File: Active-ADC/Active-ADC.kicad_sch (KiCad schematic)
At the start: 18 parts, among them J1 FPGA Terminal, J2 ADC Terminal, Q1 BC847, Q2 BC847, Q3 BC847

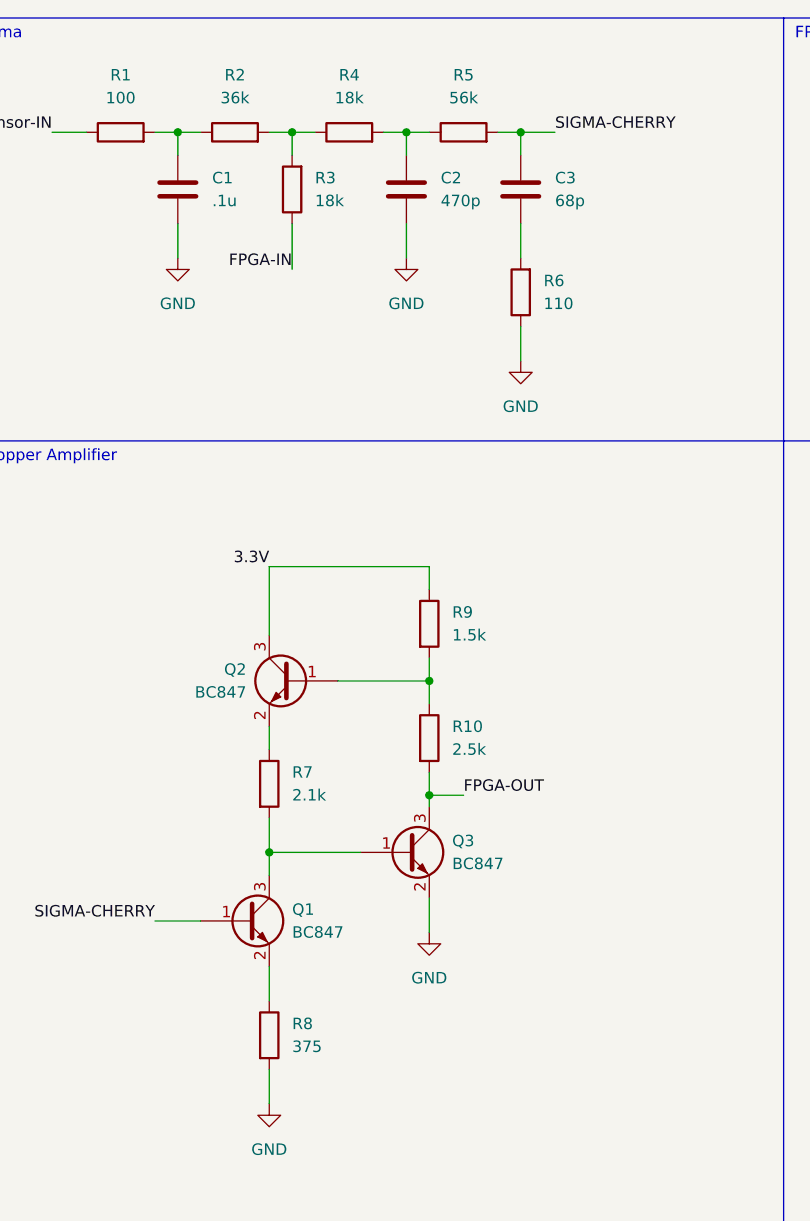
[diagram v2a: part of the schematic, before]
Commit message: Updated schematic for full SMD components with part numbers
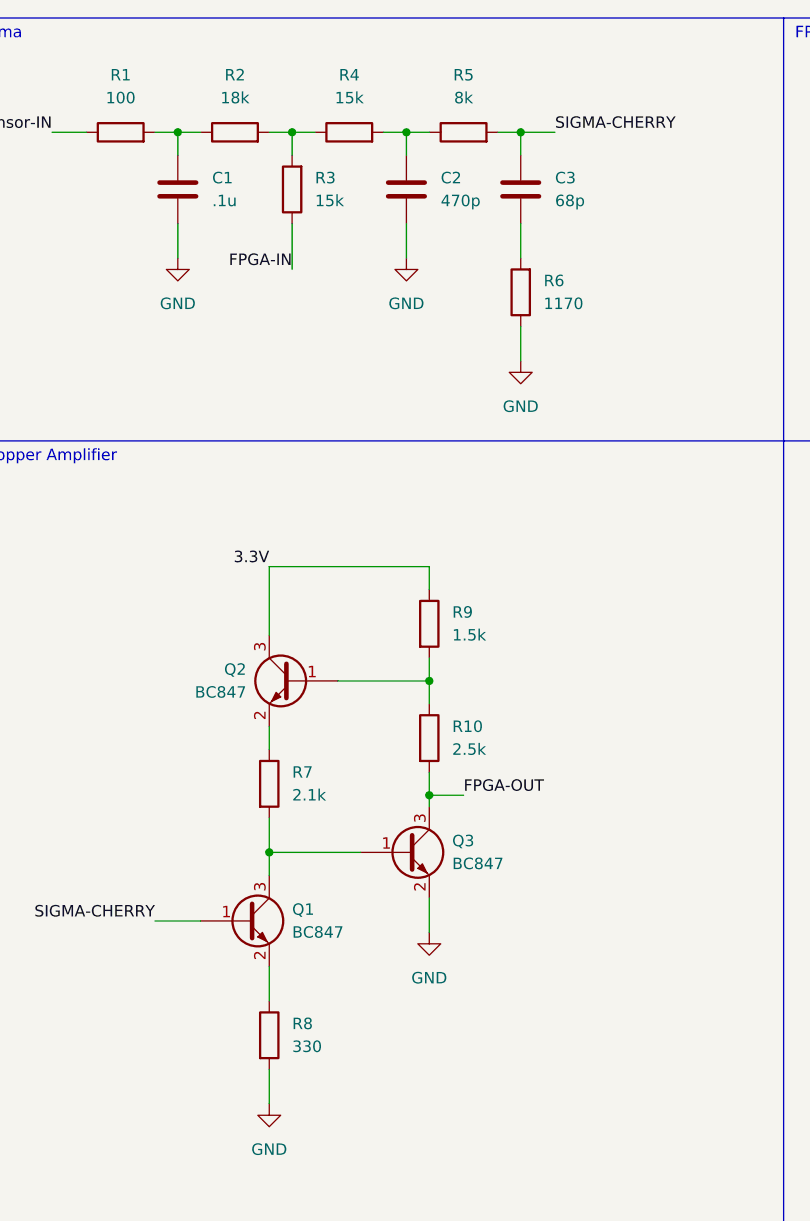
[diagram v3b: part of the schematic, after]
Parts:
- C3: footprint Capacitor_SMD:C_0402_1005Metric -> Capacitor_SMD:C_0201_0603Metric
- R10: footprint Resistor_SMD:R_0201_0603Metric -> Resistor_SMD:R_0805_2012Metric
- R2: value 36k -> 18k
- R3, R4: value 18k -> 15k
- R5: value 56k -> 8k; footprint Resistor_SMD:R_0201_0603Metric -> Resistor_SMD:R_0805_2012Metric
- R6: value 110 -> 1170
- R8: value 375 -> 330
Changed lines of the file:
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@@
     (in_bom yes) (on_board yes) (fields_autoplaced)
     (property "Reference" "R5" (id 0) (at 73.66 19.05 90))
-    (property "Value" "56k" (id 1) (at 73.66 21.59 90))
-    (property "Footprint" "Resistor_SMD:R_0201_0603Metric" (id 2) (at 73.66 27.178 90)
-      (effects (font (size 1.27 1.27)) hide)
-    )
-    (property "Datasheet" "P123347TR-ND" (id 3) (at 73.66 25.4 0)
+    (property "Value" "8k" (id 1) (at 73.66 21.59 90))
+    (property "Footprint" "Resistor_SMD:R_0805_2012Metric" (id 2) (at 73.66 27.178 90)
+      (effects (font (size 1.27 1.27)) hide)
+    )
+    (property "Datasheet" "Y1629-8.00KATR-ND" (id 3) (at 73.66 25.4 0)
       (effects (font (size 1.27 1.27)) hide)
     )
@@
       (effects (font (size 1.27 1.27)) (justify left))
     )
-    (property "Footprint" "Resistor_SMD:R_0201_0603Metric" (id 2) (at 68.072 92.71 90)
-      (effects (font (size 1.27 1.27)) hide)
-    )
-    (property "Datasheet" "~" (id 3) (at 69.85 92.71 0)
+    (property "Footprint" "Resistor_SMD:R_0805_2012Metric" (id 2) (at 68.072 92.71 90)
+      (effects (font (size 1.27 1.27)) hide)
+    )
+    (property "Datasheet" "Y1629-2.50KATR-ND" (id 3) (at 69.85 92.71 0)
       (effects (font (size 1.27 1.27)) hide)
     )
@@
       (effects (font (size 1.27 1.27)) hide)
     )
-    (property "Datasheet" "~" (id 3) (at 69.85 80.01 0)
+    (property "Datasheet" "1292-WR06X152JTLTR-ND" (id 3) (at 69.85 80.01 0)
       (effects (font (size 1.27 1.27)) hide)
     )
@@
     (in_bom yes) (on_board yes) (fields_autoplaced)
     (property "Reference" "R4" (id 0) (at 60.96 19.05 90))
-    (property "Value" "18k" (id 1) (at 60.96 21.59 90))
+    (property "Value" "15k" (id 1) (at 60.96 21.59 90))
     (property "Footprint" "Resistor_SMD:R_0201_0603Metric" (id 2) (at 60.96 27.178 90)
       (effects (font (size 1.27 1.27)) hide)
     )
-    (property "Datasheet" "311-18.0KMTR-ND" (id 3) (at 60.96 25.4 0)
+    (property "Datasheet" "1292-WR06X153JTLTR-ND" (id 3) (at 60.96 25.4 0)
       (effects (font (size 1.27 1.27)) hide)
     )
@@
       (effects (font (size 1.27 1.27)) (justify left))
     )
-    (property "Value" "375" (id 1) (at 54.61 126.9999 0)
+    (property "Value" "330" (id 1) (at 54.61 126.9999 0)
       (effects (font (size 1.27 1.27)) (justify left))
     )
@@
       (effects (font (size 1.27 1.27)) hide)
     )
-    (property "Datasheet" "~" (id 3) (at 52.07 125.73 0)
+    (property "Datasheet" "1292-WR06X331JTLTR-ND" (id 3) (at 52.07 125.73 0)
       (effects (font (size 1.27 1.27)) hide)
     )
@@
       (effects (font (size 1.27 1.27)) (justify right))
     )
-    (property "Value" "110" (id 1) (at 82.55 44.4499 0)
+    (property "Value" "1170" (id 1) (at 82.55 44.4499 0)
       (effects (font (size 1.27 1.27)) (justify right))
     )
@@
       (effects (font (size 1.27 1.27)) hide)
     )
-    (property "Datasheet" "YAG2379TR-ND" (id 3) (at 80.01 43.18 0)
+    (property "Datasheet" "2019-RN73R1JTTD1171B10TR-ND" (id 3) (at 80.01 43.18 0)
       (effects (font (size 1.27 1.27)) hide)
     )
@@
       (effects (font (size 1.27 1.27)) (justify right))
     )
-    (property "Value" "18k" (id 1) (at 57.15 33.0199 0)
+    (property "Value" "15k" (id 1) (at 57.15 33.0199 0)
       (effects (font (size 1.27 1.27)) (justify right))
     )
@@
       (effects (font (size 1.27 1.27)) hide)
     )
-    (property "Datasheet" "311-18.0KMTR-ND" (id 3) (at 54.61 31.75 0)
+    (property "Datasheet" "1292-WR06X153JTLTR-ND" (id 3) (at 54.61 31.75 0)
       (effects (font (size 1.27 1.27)) hide)
     )
@@
     (in_bom yes) (on_board yes) (fields_autoplaced)
     (property "Reference" "R2" (id 0) (at 48.26 19.05 90))
-    (property "Value" "36k" (id 1) (at 48.26 21.59 90))
+    (property "Value" "18k" (id 1) (at 48.26 21.59 90))
     (property "Footprint" "Resistor_SMD:R_0201_0603Metric" (id 2) (at 48.26 27.178 90)
       (effects (font (size 1.27 1.27)) hide)
     )
-    (property "Datasheet" "YAG2626TR-ND" (id 3) (at 48.26 25.4 0)
+    (property "Datasheet" "311-18.0KMTR-ND" (id 3) (at 48.26 25.4 0)
       (effects (font (size 1.27 1.27)) hide)
     )
@@
       (effects (font (size 1.27 1.27)) (justify left))
     )
-    (property "Footprint" "Capacitor_SMD:C_0402_1005Metric" (id 2) (at 80.9752 35.56 0)
-      (effects (font (size 1.27 1.27)) hide)
-    )
-    (property "Datasheet" "478-1080-2-ND" (id 3) (at 80.01 31.75 0)
+    (property "Footprint" "Capacitor_SMD:C_0201_0603Metric" (id 2) (at 80.9752 35.56 0)
+      (effects (font (size 1.27 1.27)) hide)
+    )
+    (property "Datasheet" "1292-1542-2-ND" (id 3) (at 80.01 31.75 0)
       (effects (font (size 1.27 1.27)) hide)
     )
@@
       (effects (font (size 1.27 1.27)) hide)
     )
-    (property "Datasheet" "~" (id 3) (at 52.07 97.79 0)
+    (property "Datasheet" "311-2.10KHRTR-ND" (id 3) (at 52.07 97.79 0)
       (effects (font (size 1.27 1.27)) hide)
     )
@@
     )
     (path "/dd02a207-fa49-45c1-8a6d-f9dc54a91fee"
-      (reference "C3") (unit 1) (value "68p") (footprint "Capacitor_SMD:C_0402_1005Metric")
+      (reference "C3") (unit 1) (value "68p") (footprint "Capacitor_SMD:C_0201_0603Metric")
     )
     (path "/fbc3ac75-825f-438a-85e7-381ae2adaad7"
@@
     )
     (path "/a4a8430c-d7a1-47ce-bbb3-0b02aed0c1eb"
-      (reference "R2") (unit 1) (value "36k") (footprint "Resistor_SMD:R_0201_0603Metric")
+      (reference "R2") (unit 1) (value "18k") (footprint "Resistor_SMD:R_0201_0603Metric")
     )
     (path "/88afc6d6-80c2-449c-adb0-b4bcf7eec011"
-      (reference "R3") (unit 1) (value "18k") (footprint "Resistor_SMD:R_0201_0603Metric")
+      (reference "R3") (unit 1) (value "15k") (footprint "Resistor_SMD:R_0201_0603Metric")
     )
     (path "/699138f6-237a-4b8a-a4d4-7fb9091d901b"
-      (reference "R4") (unit 1) (value "18k") (footprint "Resistor_SMD:R_0201_0603Metric")
+      (reference "R4") (unit 1) (value "15k") (footprint "Resistor_SMD:R_0201_0603Metric")
     )
     (path "/0456c7de-9f79-46f5-a17e-4fa13a1b0cfc"
-      (reference "R5") (unit 1) (value "56k") (footprint "Resistor_SMD:R_0201_0603Metric")
+      (reference "R5") (unit 1) (value "8k") (footprint "Resistor_SMD:R_0805_2012Metric")
     )
     (path "/84aecc63-06ed-478f-8f5f-d0d1edf5fbec"
-      (reference "R6") (unit 1) (value "110") (footprint "Resistor_SMD:R_0201_0603Metric")
+      (reference "R6") (unit 1) (value "1170") (footprint "Resistor_SMD:R_0201_0603Metric")
     )
     (path "/f2a977c8-30ef-4319-82c2-32f34a4a3175"
@@
     )
     (path "/745cd236-ebd5-45a2-9f15-f3ef3d7dae9c"
-      (reference "R8") (unit 1) (value "375") (footprint "Resistor_SMD:R_0201_0603Metric")
+      (reference "R8") (unit 1) (value "330") (footprint "Resistor_SMD:R_0201_0603Metric")
     )
     (path "/38d17884-57d2-4dc7-9a53-9bb47fd2d837"
@@
     )
     (path "/2b56ea83-9e8a-4d22-a128-e140e248933c"
-      (reference "R10") (unit 1) (value "2.5k") (footprint "Resistor_SMD:R_0201_0603Metric")
-    )
-  )
+      (reference "R10") (unit 1) (value "2.5k") (footprint "Resistor_SMD:R_0805_2012Metric")
+    )
+  )

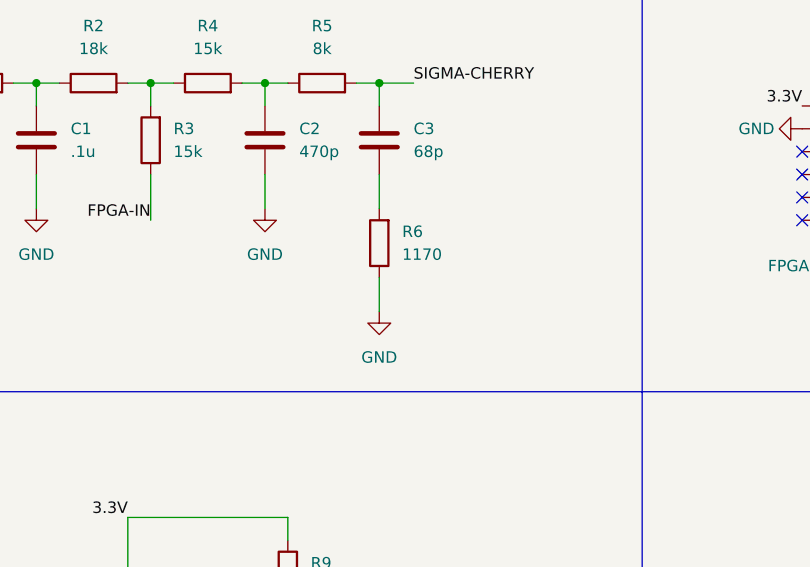
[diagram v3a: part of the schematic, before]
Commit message: Updated footprints too all 0805 standard
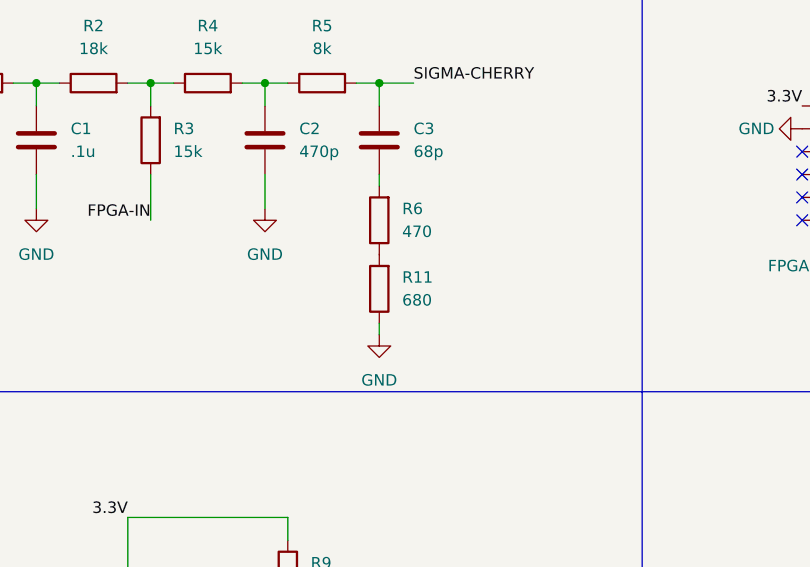
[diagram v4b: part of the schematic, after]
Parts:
- added R11: 680, Resistor_SMD:R_0805_2012Metric_Pad1.20x1.40mm_HandSolder, symbol Device:R
- C1, C2, C3: footprint Capacitor_SMD:C_0201_0603Metric -> Capacitor_SMD:C_0805_2012Metric_Pad1.18x1.45mm_HandSolder
- R1, R2, R3, R4, R7, R8, R9: footprint Resistor_SMD:R_0201_0603Metric -> Resistor_SMD:R_0805_2012Metric_Pad1.20x1.40mm_HandSolder
- R10, R5: footprint Resistor_SMD:R_0805_2012Metric -> Resistor_SMD:R_0805_2012Metric_Pad1.20x1.40mm_HandSolder
- R6: value 1170 -> 470; footprint Resistor_SMD:R_0201_0603Metric -> Resistor_SMD:R_0805_2012Metric_Pad1.20x1.40mm_HandSolder
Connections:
- net GND: now also R11.1; no longer R6.1
- new net: R11.2, R6.1
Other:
- moved on the sheet: R6

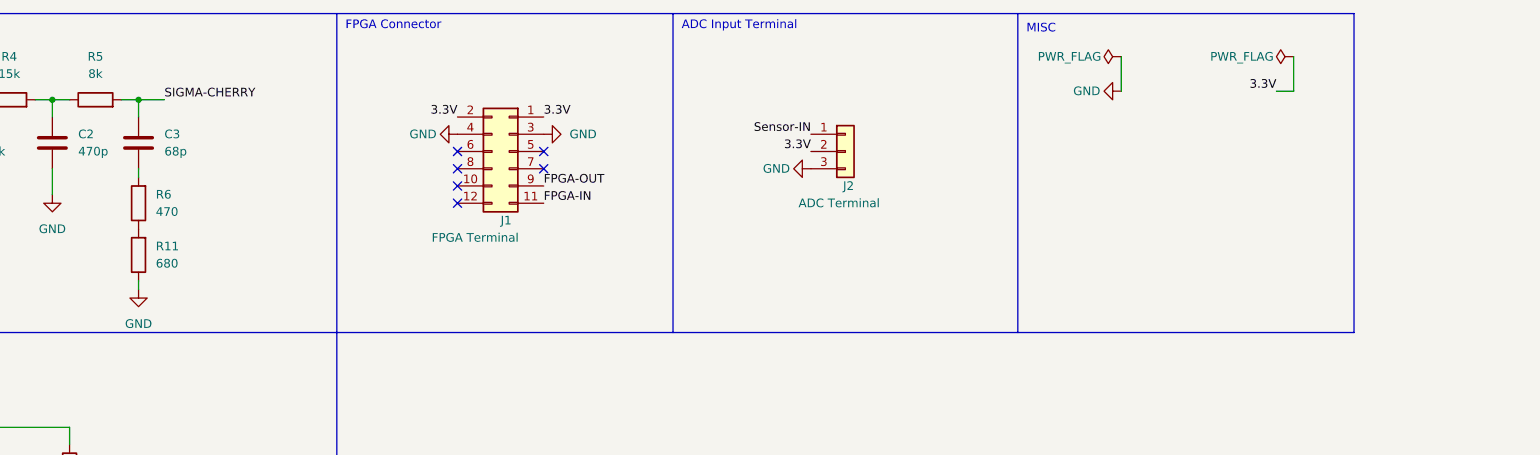
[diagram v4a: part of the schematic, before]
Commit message: Close to final pcb adjusted footprints and layout design incorperating voltage divider
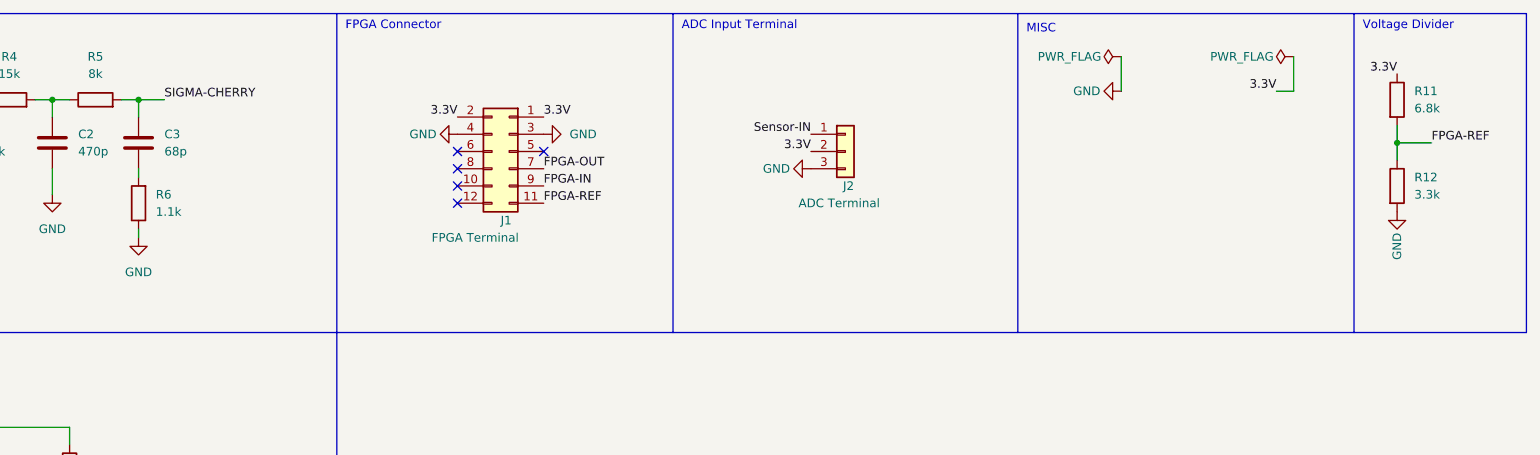
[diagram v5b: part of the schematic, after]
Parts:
- added R12: 3.3k, Resistor_SMD:R_0805_2012Metric_Pad1.20x1.40mm_HandSolder, symbol Device:R
- J1: footprint PinHeader_2x06_P1.00mm_Horizontal -> Connector_PinHeader_2.54mm:PinHeader_2x06_P2.54mm_Horizontal
- J2: footprint PinHeader_1x03_P1.00mm_Vertical -> Connector_PinHeader_2.54mm:PinHeader_1x03_P2.54mm_Vertical
- R11: value 680 -> 6.8k
- R6: value 470 -> 1.1k
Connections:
- net 3.3V: now also R11.1
- net FPGA-IN: now also J1.9 (Pin_9); no longer J1.11 (Pin_11)
- net FPGA-OUT: now also J1.7 (Pin_7); no longer J1.9 (Pin_9)
- net GND: now also R6.1, R12.2; no longer R11.1
- net FPGA-REF: now reaches R11.2
- net FPGA-REF: now also J1.11 (Pin_11), R12.1; no longer R6.1
- no-connect marks 6 -> 5
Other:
- note added: "Voltage Divider"

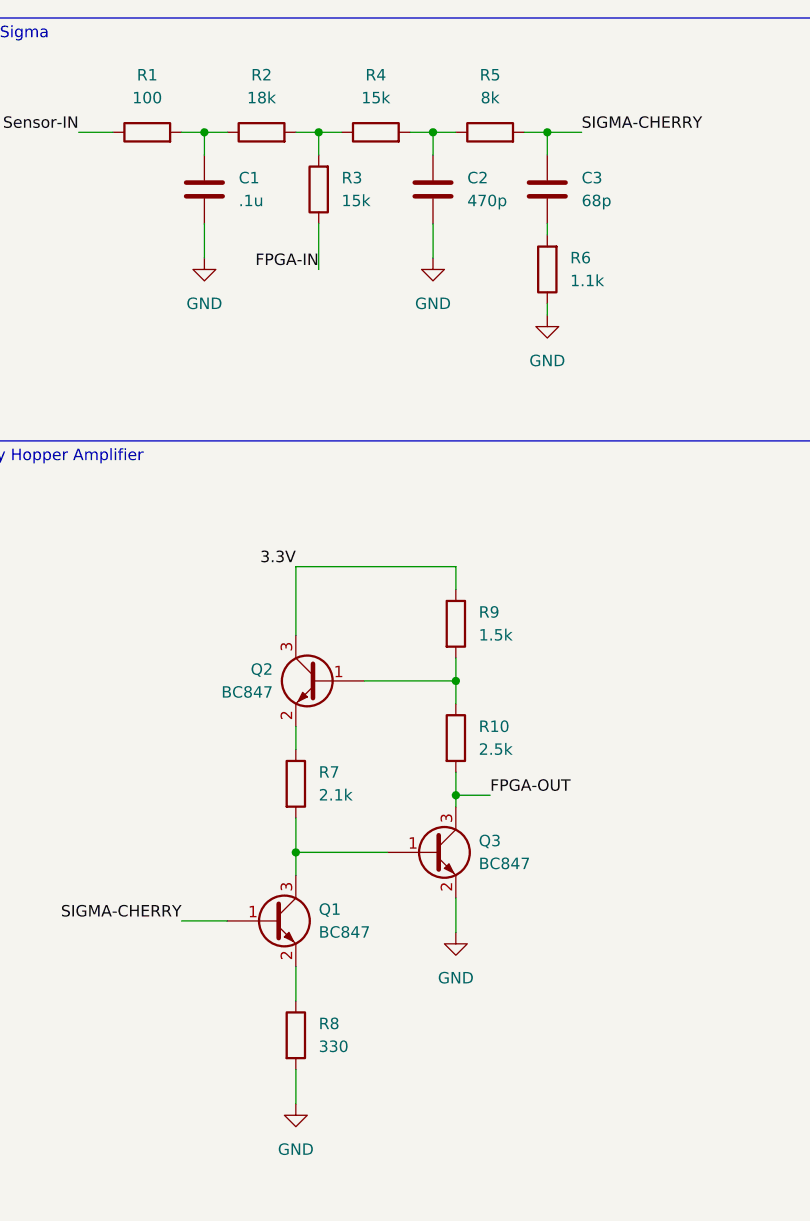
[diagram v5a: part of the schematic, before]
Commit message: Updated models with new schematic details
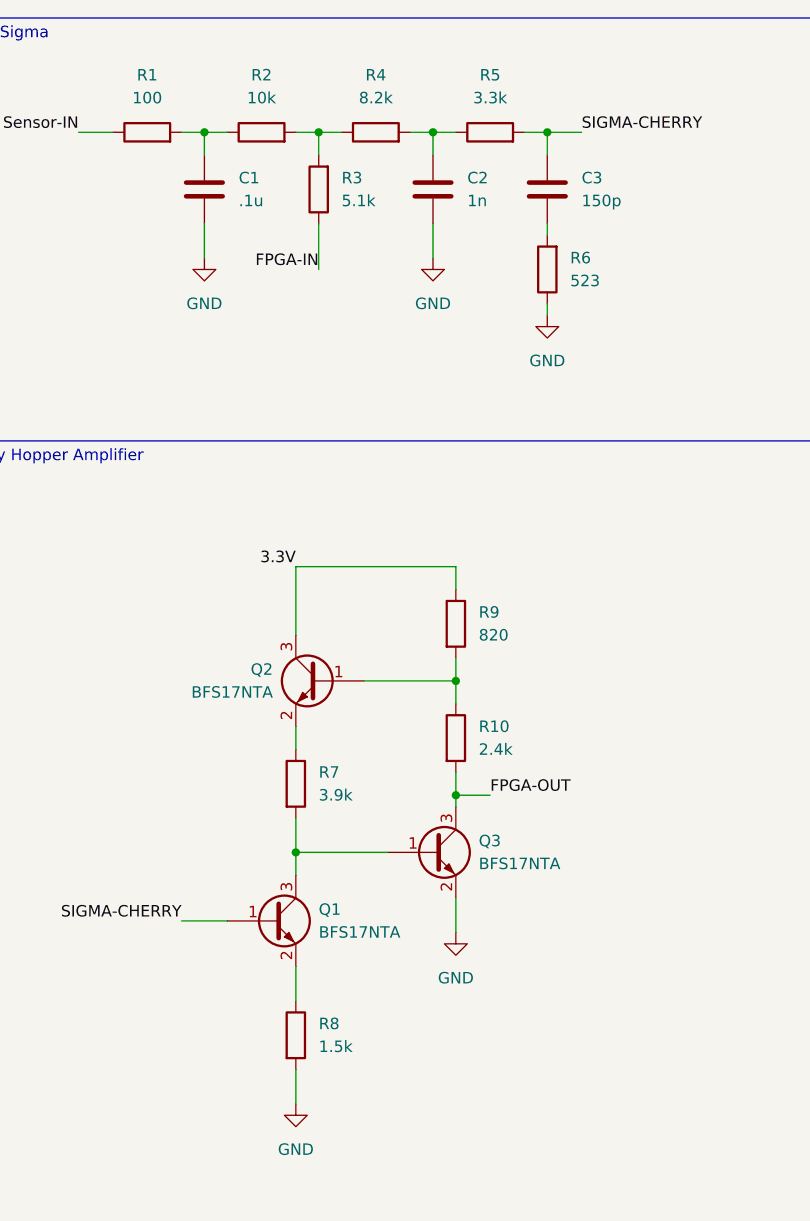
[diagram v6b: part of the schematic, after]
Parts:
- C2: value 470p -> 1n
- C3: value 68p -> 150p
- Q1, Q2, Q3: value BC847 -> BFS17NTA
- R10: value 2.5k -> 2.4k
- R2: value 18k -> 10k
- R3: value 15k -> 5.1k
- R4: value 15k -> 8.2k
- R5: value 8k -> 3.3k
- R6: value 1.1k -> 523
- R7: value 2.1k -> 3.9k
- R8: value 330 -> 1.5k
- R9: value 1.5k -> 820
